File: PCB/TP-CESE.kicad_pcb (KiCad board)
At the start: 2 copper layers, 37 parts, among them J1 Screw_Terminal_01x04, J3 Screw_Terminal_01x02, J4 Conn_01x04_Male, J5 test, Q1 IRF540N, Q2 IRF540N, Q3 IRF540N, Q4 IRF540N, U1 4N25, U2 4N25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

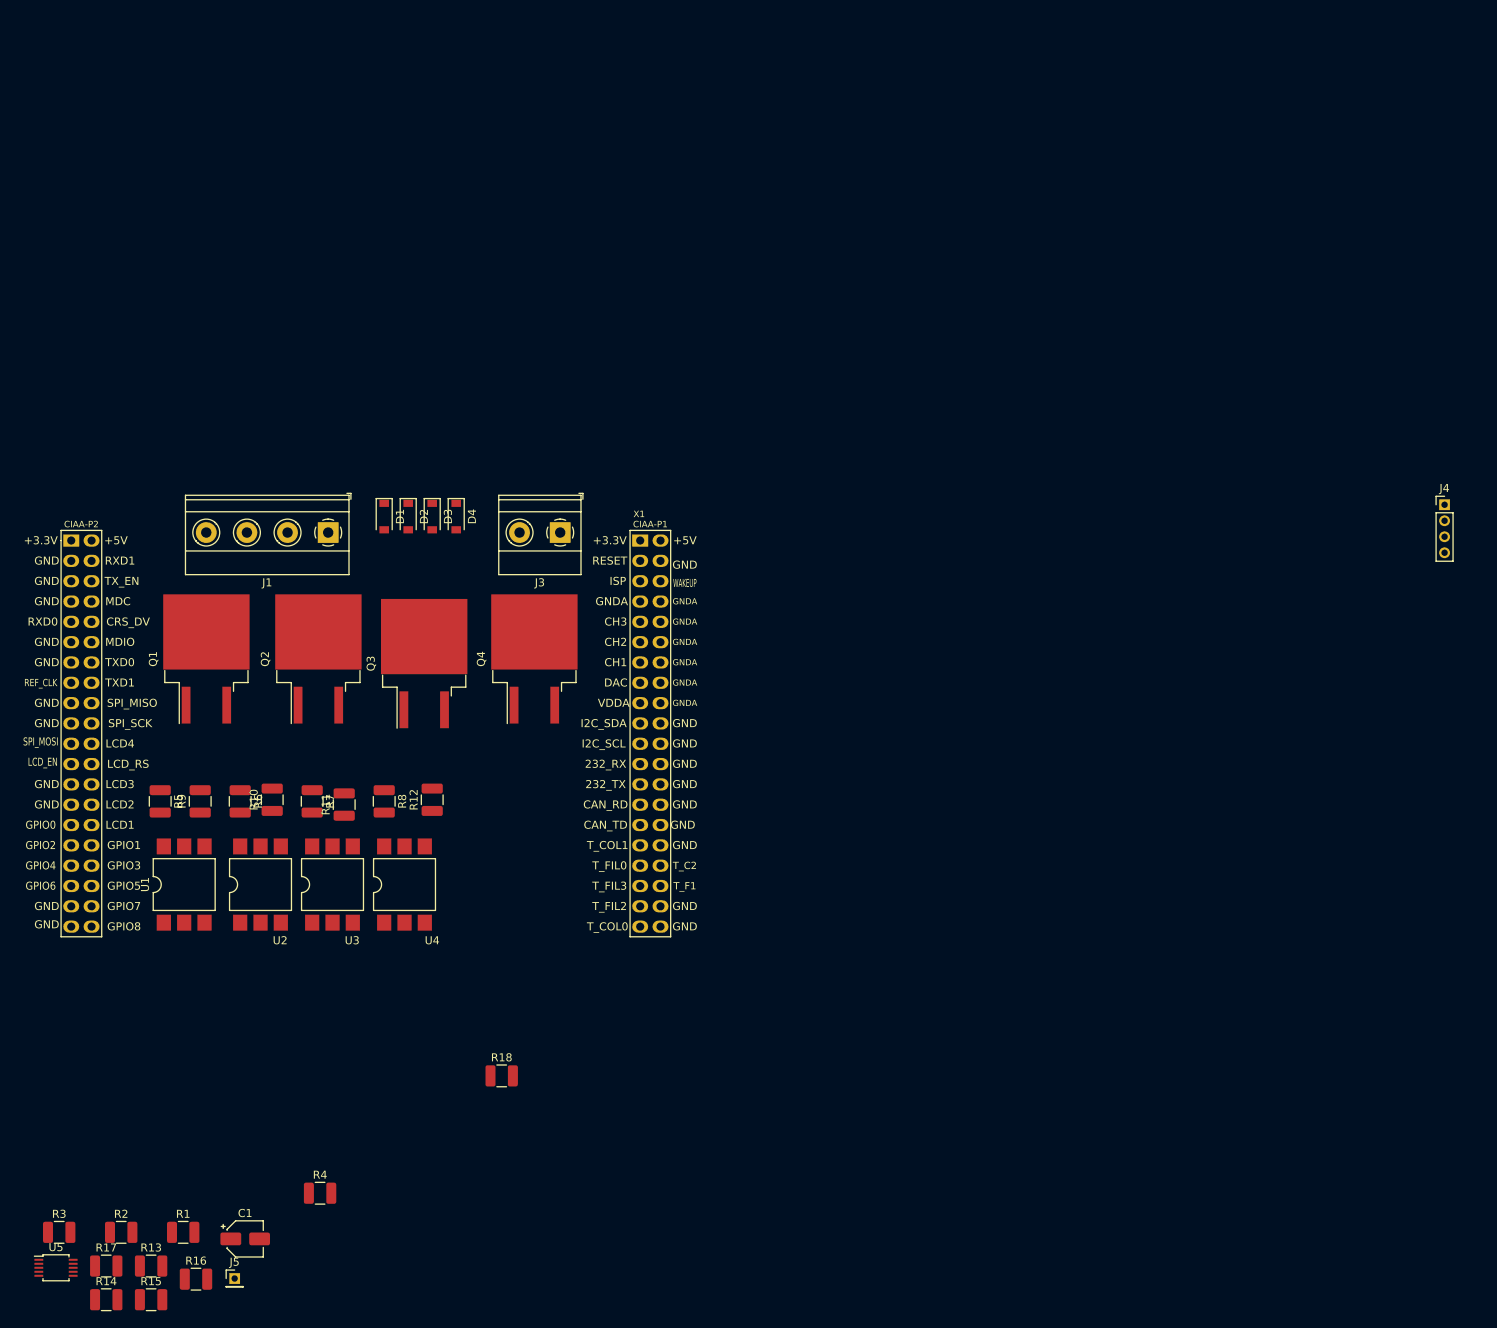
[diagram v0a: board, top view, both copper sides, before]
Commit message: Correciones al esquematico, de acuerdo a sugerencia de Diego Brengi(Profesor)  y Carlos Carreño Romano(revisor)
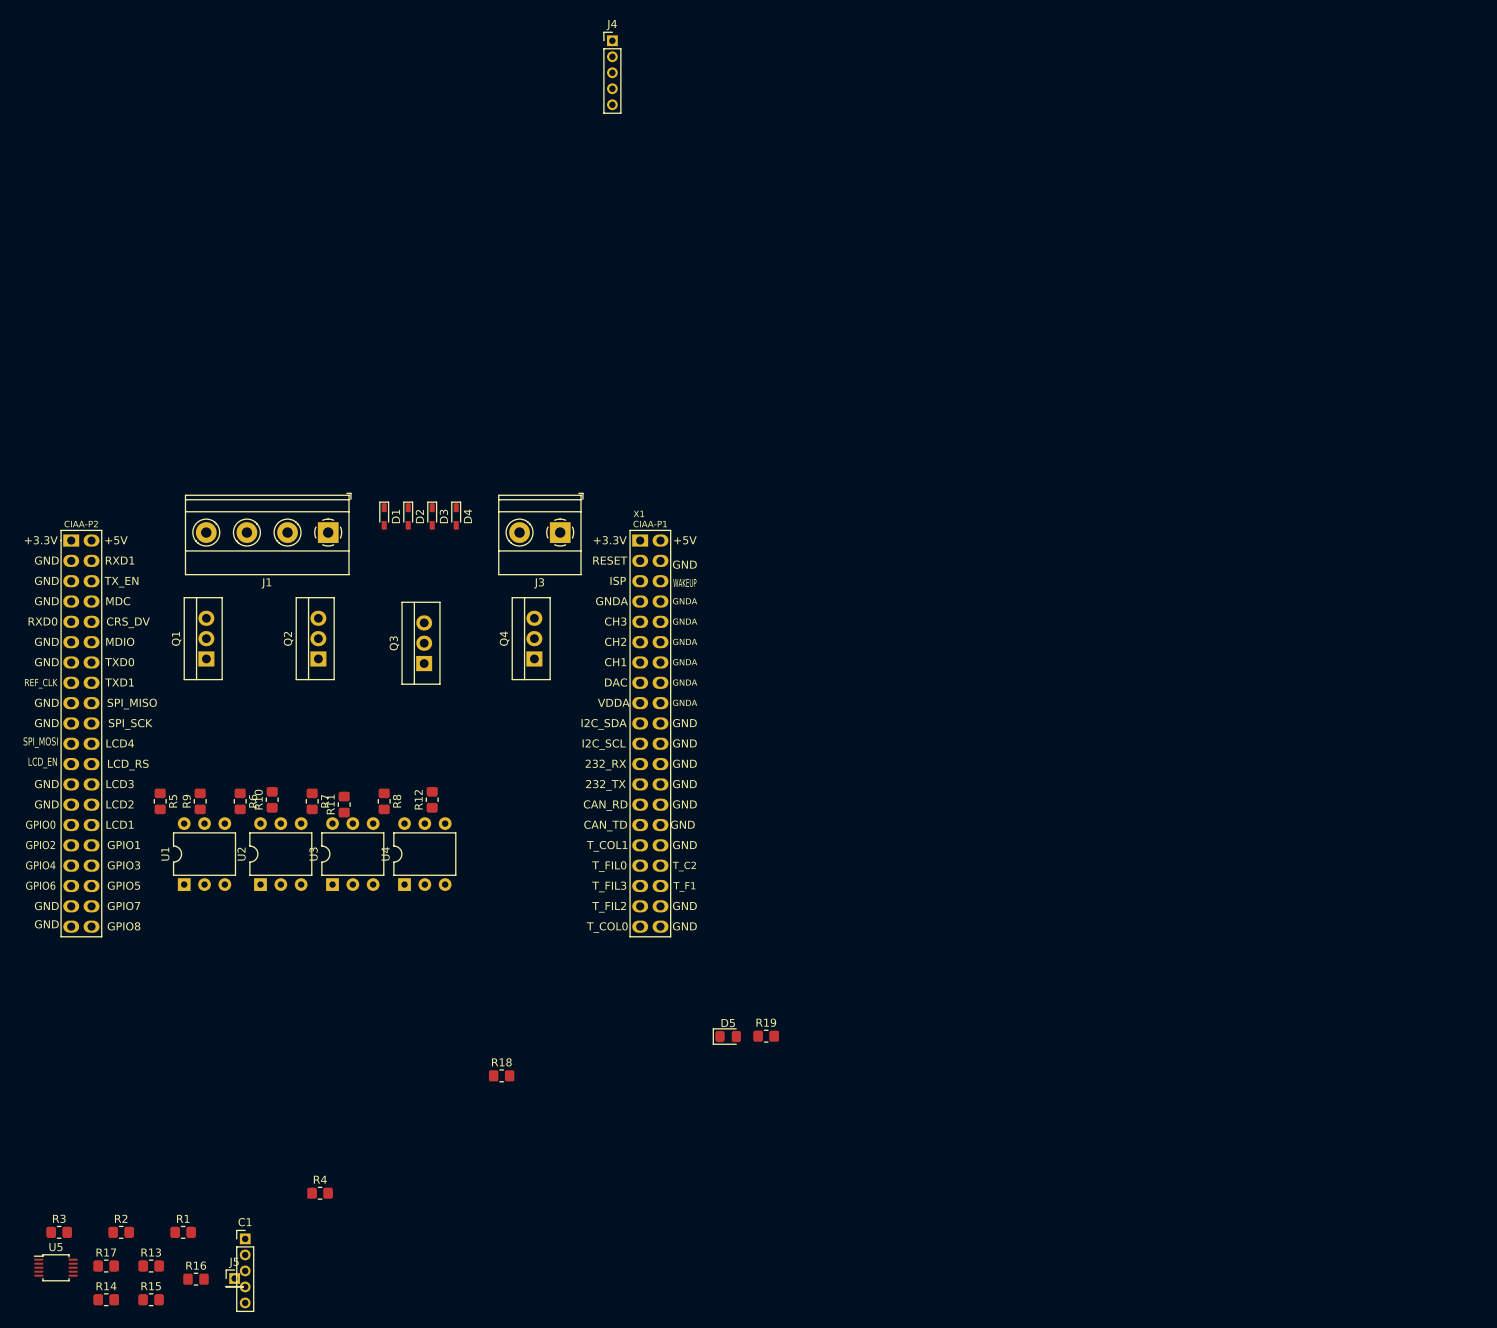
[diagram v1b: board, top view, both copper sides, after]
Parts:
- added D5: LED, LED_SMD:LED_0805_2012Metric_Pad1.15x1.40mm_HandSolder, F.Cu at (157.0, 123.0)
- added R19: 470, Resistor_SMD:R_0805_2012Metric_Pad1.20x1.40mm_HandSolder, F.Cu at (161.7, 123.0)
- C1: footprint Capacitor_SMD:CP_Elec_4x5.4 -> Connector_PinHeader_2.00mm:PinHeader_1x05_P2.00mm_Vertical
- D1, D2, D3, D4: value D -> 1N4148; footprint Diode_SMD:D_SOD-123 -> Diode_SMD:D_SC-80_HandSoldering
- J4: value Conn_01x04_Male -> Conn_01x05_Male; footprint Connector_PinHeader_2.00mm:PinHeader_1x04_P2.00mm_Vertical -> Connector_PinHeader_2.00mm:PinHeader_1x05_P2.00mm_Vertical
- Q1, Q2, Q3, Q4: footprint Package_TO_SOT_SMD:TO-263-2 -> Package_TO_SOT_THT:TO-262-3_Vertical
- R1, R10, R11, R12, R13, R14, R15, R16, R17, R18, R2, R3, R4, R5, R6, R7, R8, R9: footprint Resistor_SMD:R_1210_3225Metric -> Resistor_SMD:R_0805_2012Metric_Pad1.20x1.40mm_HandSolder
- U1, U2, U3, U4: footprint Package_DIP:SMDIP-6_W9.53mm -> Package_DIP:DIP-6_W7.62mm
- moved J4 119.1 mm to (142.5, -1.47)
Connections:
- net Net-(C1-Pad1) renamed +3V3
- net VCC renamed +5VP
- J4 pad 1: Net-(J4-Pad1) -> GND
- U5 pad 4: Net-(J4-Pad1) -> Net-(J4-Pad5)
- U5 pad 5: Net-(J4-Pad2) -> Net-(J4-Pad4)
- U5 pad 7: Net-(J4-Pad4) -> Net-(J4-Pad2)
- X1 pad 10: Net-(X1-Pad10) -> GND
- X1 pad 12: Net-(X1-Pad12) -> GND
- X1 pad 14: Net-(X1-Pad14) -> GND
- X1 pad 16: Net-(X1-Pad16) -> GND
- X1 pad 18: Net-(X1-Pad18) -> GND
- X1 pad 20: Net-(X1-Pad20) -> GND
- X1 pad 22: Net-(X1-Pad22) -> GND
- X1 pad 24: Net-(X1-Pad24) -> GND
- X1 pad 26: Net-(X1-Pad26) -> GND
- X1 pad 28: Net-(X1-Pad28) -> GND
- X1 pad 30: Net-(X1-Pad30) -> GND
- X1 pad 32: Net-(X1-Pad32) -> GND
- X1 pad 38: Net-(X1-Pad38) -> GND
- X1 pad 4: Net-(X1-Pad4) -> GND
- X1 pad 40: Net-(X1-Pad40) -> GND
- X1 pad 43: Net-(X1-Pad43) -> GND
- X1 pad 45: Net-(X1-Pad45) -> GND
- X1 pad 47: Net-(X1-Pad47) -> GND
- X1 pad 51: Net-(X1-Pad51) -> GND
- X1 pad 53: Net-(X1-Pad53) -> GND
- X1 pad 57: Net-(X1-Pad57) -> GND
- X1 pad 59: Net-(X1-Pad59) -> GND
- X1 pad 65: Net-(X1-Pad65) -> GND
- X1 pad 67: Net-(X1-Pad67) -> GND
- X1 pad 7: Net-(X1-Pad7) -> GND
- X1 pad 77: Net-(X1-Pad77) -> GND
- X1 pad 79: Net-(X1-Pad79) -> GND
- X1 pad 8: Net-(X1-Pad8) -> GND

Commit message: Posicionamiento de componenetes en PCB
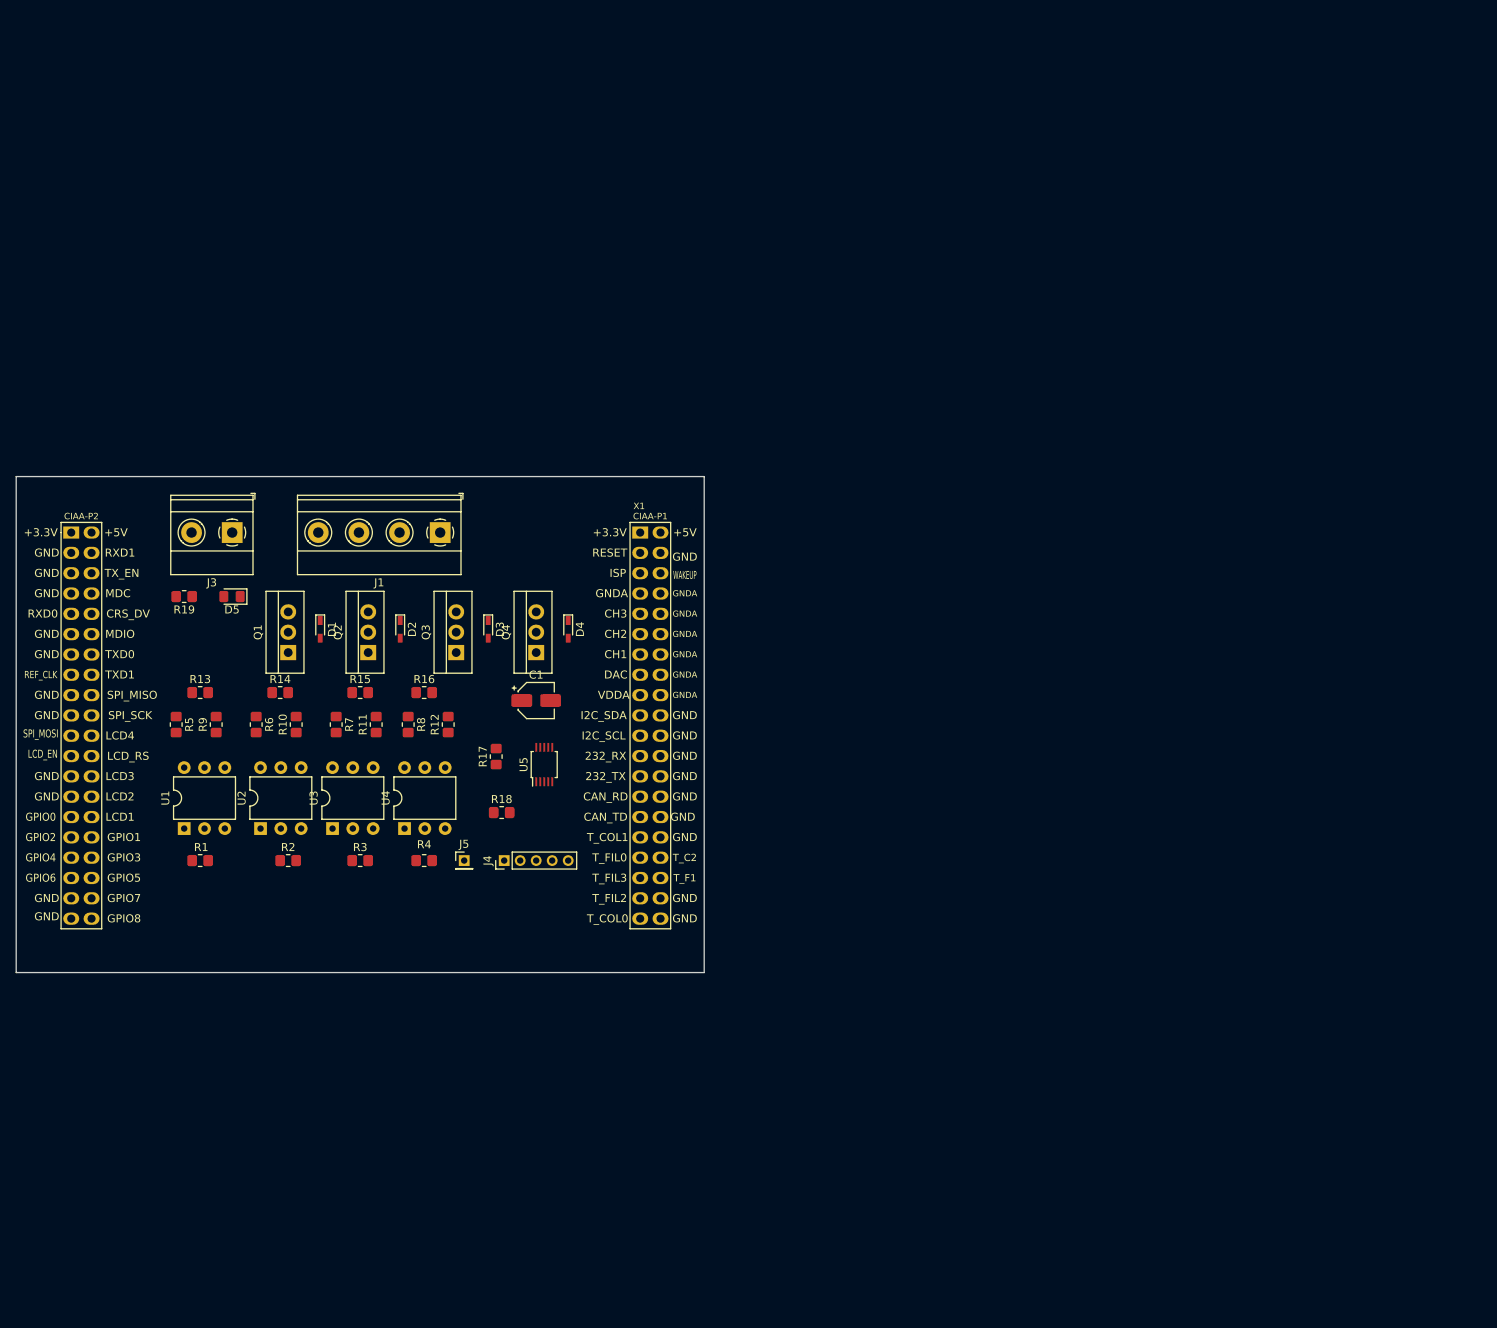
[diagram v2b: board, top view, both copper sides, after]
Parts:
- C1: footprint Connector_PinHeader_2.00mm:PinHeader_1x05_P2.00mm_Vertical -> Capacitor_SMD:CP_Elec_4x4.5
- moved J4 103.4 mm to (129.0, 101.0), turned to 90 degrees
- moved R19 91.2 mm to (89.0, 68.0), turned to 180 degrees
- moved U5 87.6 mm to (134.0, 89.0), turned to 90 degrees
- moved D5 82.9 mm to (95.0, 68.0), turned to 180 degrees
- moved R15 80.3 mm to (111.0, 80.0)
- moved R17 80.2 mm to (128.0, 88.0), turned to 90 degrees
- moved R14 78.9 mm to (101.0, 80.0)
- moved R16 78.7 mm to (119.0, 80.0)
- moved C1 76.5 mm to (133.0, 81.0)
- moved R13 71.9 mm to (91.0, 80.0)
- moved R3 59.8 mm to (111.0, 101.0)
- moved J5 59.6 mm to (124.0, 101.0)
- moved R2 50.9 mm to (102.0, 101.0)
- moved R1 46.5 mm to (91.0, 101.0)
- moved R4 43.6 mm to (119.0, 101.0)
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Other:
- board outline added: 86 x 62 mm
- net class Default: clearance 0.2 -> 0.8
- rule trace_clearance: 0.2 -> 0.8

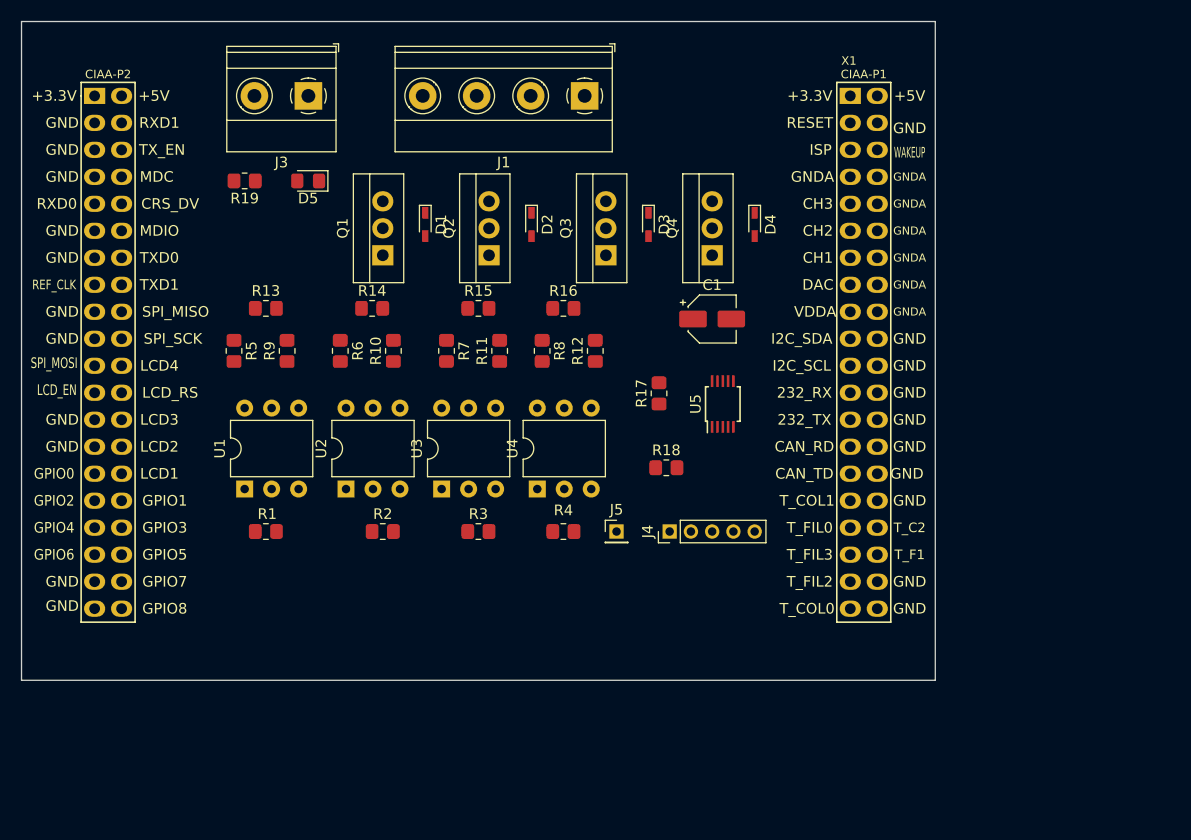
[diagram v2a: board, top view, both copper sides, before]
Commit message: Ubicacion de componentes y ruteados
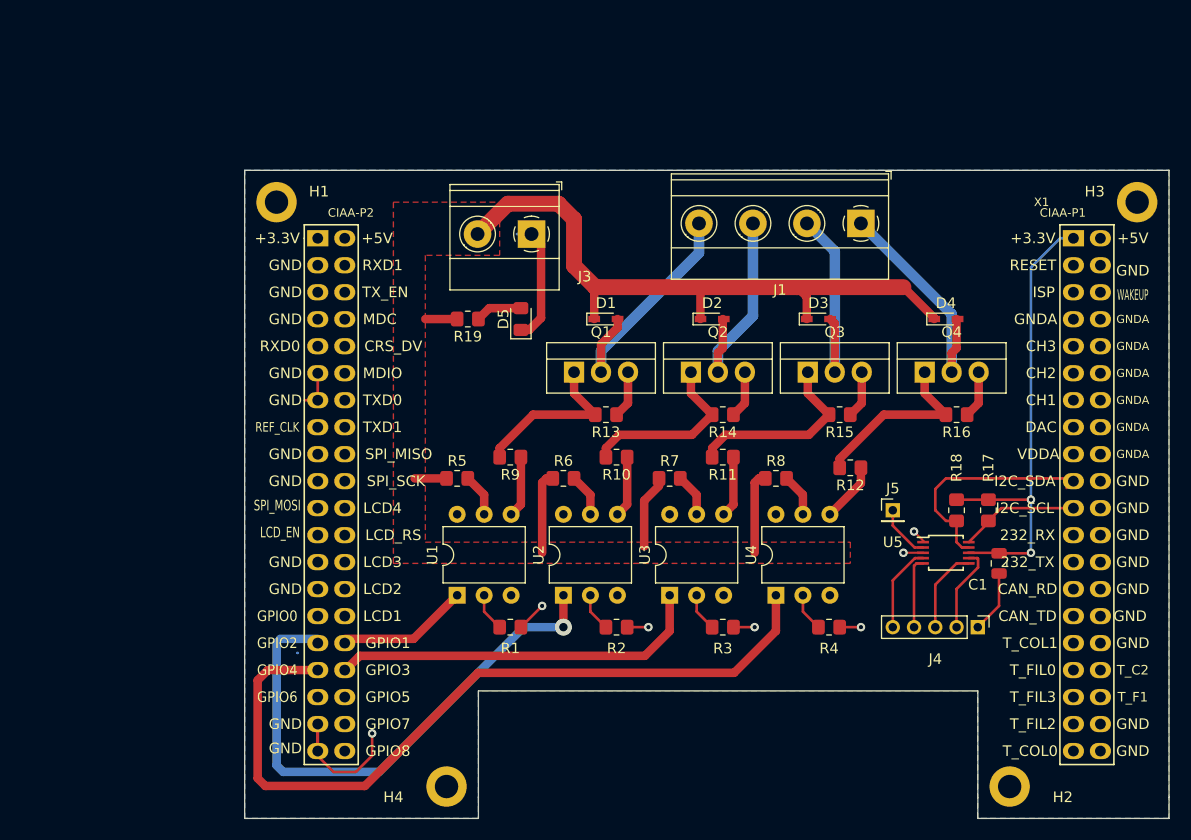
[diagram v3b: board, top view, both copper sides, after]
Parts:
- added H1: MountingHole, MountingHole:MountingHole_2.2mm_M2_DIN965_Pad, F.Cu at (92.0, 70.0)
- added H2: MountingHole, MountingHole:MountingHole_2.2mm_M2_DIN965_Pad, F.Cu at (161.0, 125.0)
- added H3: MountingHole, MountingHole:MountingHole_2.2mm_M2_DIN965_Pad, F.Cu at (173.0, 70.0)
- added H4: MountingHole, MountingHole:MountingHole_2.2mm_M2_DIN965_Pad, F.Cu at (108.0, 125.0)
- C1: value 1 uf -> 0,1 uf; footprint Capacitor_SMD:CP_Elec_4x4.5 -> Capacitor_SMD:C_0805_2012Metric
- moved R16 38.3 mm to (156.0, 90.0), turned to 180 degrees
- moved C1 35.5 mm to (160.0, 104.0), turned to 270 degrees
- moved R15 35.4 mm to (145.0, 90.0), turned to 180 degrees
- moved R14 34.5 mm to (134.0, 90.0), turned to 180 degrees
- moved R13 33.5 mm to (123.0, 90.0), turned to 180 degrees
- moved R17 32.9 mm to (159.0, 99.0)
- moved J4 30.4 mm to (158.0, 110.0), turned to 270 degrees
- moved J1 28.6 mm to (147.0, 72.0)
- moved R18 27.6 mm to (156.0, 99.0), turned to 270 degrees
- moved R4 26.6 mm to (144.0, 110.0)
- moved R12 26.4 mm to (146.0, 95.0), turned to 180 degrees
- moved J5 26.1 mm to (150.0, 99.0)
- moved U5 25.2 mm to (155.0, 103.0), turned to 0 degrees
- moved R8 25.1 mm to (139.0, 96.0), turned to 0 degrees
- moved X1 24.9 mm to (167.0, 73.4)
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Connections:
- U5 pad 10: Net-(R18-Pad2) -> Net-(R17-Pad1)
- U5 pad 9: Net-(R17-Pad1) -> Net-(R18-Pad2)
- X1 pad 19: Net-(R17-Pad1) -> Net-(R18-Pad2)
- X1 pad 21: Net-(R18-Pad2) -> Net-(R17-Pad1)
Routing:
- net +5VP: track 0.00 -> 89.3 mm
- net Net-(U4-Pad1): track 0.00 -> 73.8 mm
- net GND: track 0.00 -> 66.5 mm, vias 0 -> 7
- net Net-(U2-Pad1): track 0.00 -> 52.1 mm, vias 0 -> 1
- net +3V3: track 0.00 -> 44.9 mm, vias 0 -> 2
- net Net-(U3-Pad1): track 0.00 -> 35.3 mm
- net Net-(D1-Pad2): track 0.00 -> 23.5 mm
- net Net-(D4-Pad2): track 0.00 -> 22.9 mm
- net Net-(R18-Pad2): track 0.00 -> 22.5 mm
- net Net-(D2-Pad2): track 0.00 -> 20.6 mm
- net Net-(D3-Pad2): track 0.00 -> 20.3 mm
- net Net-(Q3-Pad1): track 0.00 -> 18.0 mm
- net Net-(Q4-Pad1): track 0.00 -> 17.4 mm
- net Net-(Q2-Pad1): track 0.00 -> 17.0 mm
- net Net-(Q1-Pad1): track 0.00 -> 16.0 mm
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- added copper zone on F.Cu, net +5VP
- added copper zone on B.Cu, net GND
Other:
- board size 86 x 62 mm -> 87 x 61 mm
- net class U5 added: clearance 0.2, trace_width 0.2, via_dia 0.8, via_drill 0.4
